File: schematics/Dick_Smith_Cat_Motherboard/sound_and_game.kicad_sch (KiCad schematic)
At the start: 24 parts, among them J8 Joystick, U34 74LS08, U39 74LS374, U42 SN76489AN, U43 74LS138, U45 74LS151, U46 NE558

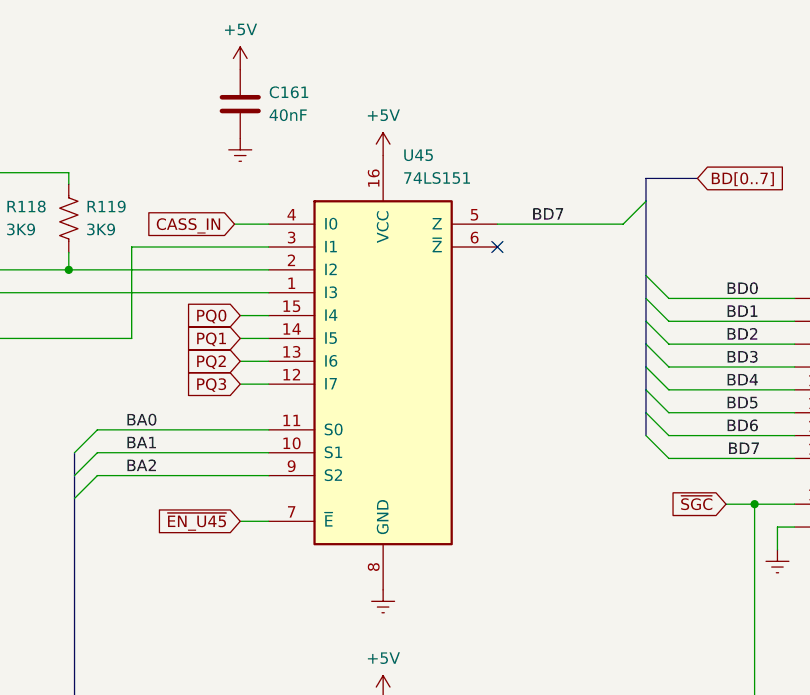
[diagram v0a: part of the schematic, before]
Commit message: Fix chip numbers in the motherboard schematic
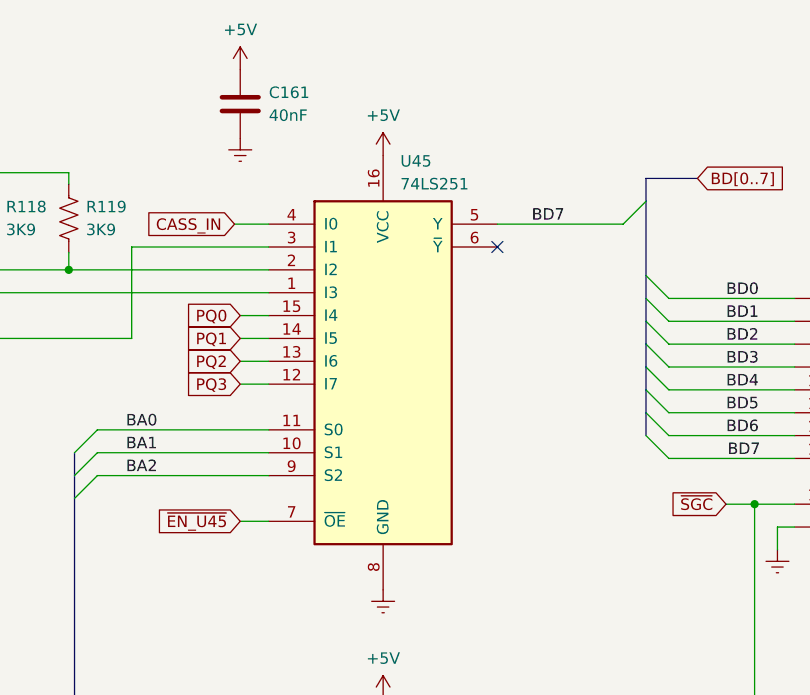
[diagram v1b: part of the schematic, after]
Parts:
- removed U45: 74LS151, Package_DIP:DIP-16_W7.62mm, symbol 74xx:74LS151
- added U45: 74LS251, Package_DIP:DIP-16_W7.62mm, symbol 74xx:74LS251
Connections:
- net +5V: now also U45.16 (VCC)
- net BA0: now also U45.11 (S0)
- net BA1: now also U45.10 (S1)
- net BA2: now also U45.9 (S2)
- net BD7: now also U45.5 (Y)
- net CASS_IN: now also U45.4 (I0)
- net Earth: now also U45.8 (GND)
- net PQ0: now also U45.15 (I4)
- net PQ1: now also U45.14 (I5)
- net PQ2: now also U45.13 (I6)
- net PQ3: now also U45.12 (I7)
- net SW0: now also U45.3 (I1)
- net SW1: now also U45.2 (I2)
- net SW2: now also U45.1 (I3)
- net ~{EN_U45}: now also U45.7 (~{OE})
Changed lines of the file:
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@@
+    )
+  )
+  (symbol (lib_id "74xx:74LS251") (at 115.57 65.405 0) (unit 1)
+    (in_bom yes) (on_board yes) (dnp no)
+    (property "Reference" "U45" (at 117.475 43.18 0)
+      (effects (font (size 1.27 1.27)) (justify left))
+    )
+    (property "Value" "74LS251" (at 117.475 45.72 0)
+      (effects (font (size 1.27 1.27)) (justify left))
+    )
+    (property "Footprint" "Package_DIP:DIP-16_W7.62mm" (at 115.57 65.405 0)
+      (effects (font (size 1.27 1.27)) hide)
+    )
+    (property "Datasheet" "http://www.ti.com/lit/gpn/sn74LS251" (at 115.57 65.405 0)
+      (effects (font (size 1.27 1.27)) hide)
+    )
+    (pin "9")
+    (pin "2")
+    (pin "11")
+    (pin "3")
+    (pin "16")
+    (pin "13")
+    (pin "1")
+    (pin "4")
+    (pin "10")
+    (pin "8")
+    (pin "7")
+    (pin "6")
+    (pin "5")
+    (pin "14")
+    (pin "15")
+    (pin "12")
+    (instances
+      (project "Dick_Smith_Cat_Motherboard"
+        (path "/b825002a-fcdd-4970-89c6-1645cf48180b/e24ea90e-b08a-42db-9a63-e0e6da1adbd2"
+          (reference "U45") (unit 1)
+        )
+      )
     )
   )
@@
         )
       )
-    )
-  )
-  (symbol (lib_id "74xx:74LS151") (at 115.57 65.405 0) (unit 1)
-    (in_bom yes) (on_board yes) (dnp no) (fields_autoplaced)
-    (property "Reference" "U45" (at 117.7641 42.545 0)
-      (effects (font (size 1.27 1.27)) (justify left))
-    )
-    (property "Value" "74LS151" (at 117.7641 45.085 0)
-      (effects (font (size 1.27 1.27)) (justify left))
-    )
-    (property "Footprint" "Package_DIP:DIP-16_W7.62mm" (at 115.57 65.405 0)
-      (effects (font (size 1.27 1.27)) hide)
-    )
-    (property "Datasheet" "http://www.ti.com/lit/gpn/sn74LS151" (at 115.57 65.405 0)
-      (effects (font (size 1.27 1.27)) hide)
-    )
-    (pin "2")
-    (pin "9")
-    (pin "10")
-    (pin "4")
-    (pin "5")
-    (pin "11")
-    (pin "16")
-    (pin "8")
-    (pin "13")
-    (pin "7")
-    (pin "12")
-    (pin "3")
-    (pin "1")
-    (pin "6")
-    (pin "14")
-    (pin "15")
-    (instances
-      (project "Dick_Smith_Cat_Motherboard"
-        (path "/b825002a-fcdd-4970-89c6-1645cf48180b/e24ea90e-b08a-42db-9a63-e0e6da1adbd2"
-          (reference "U45") (unit 1)
-        )
-      )

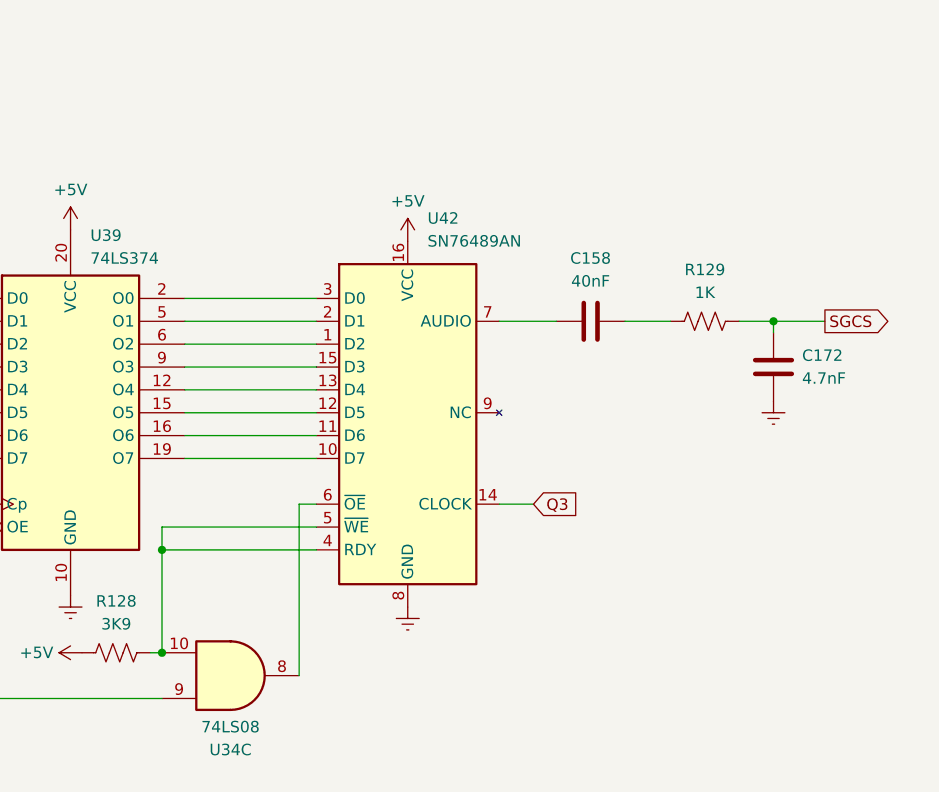
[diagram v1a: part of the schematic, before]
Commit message: Fix pinout of SN76489AN sound chip
The sound chip uses D0 as the MSB.  The bits are swapped in hardware.
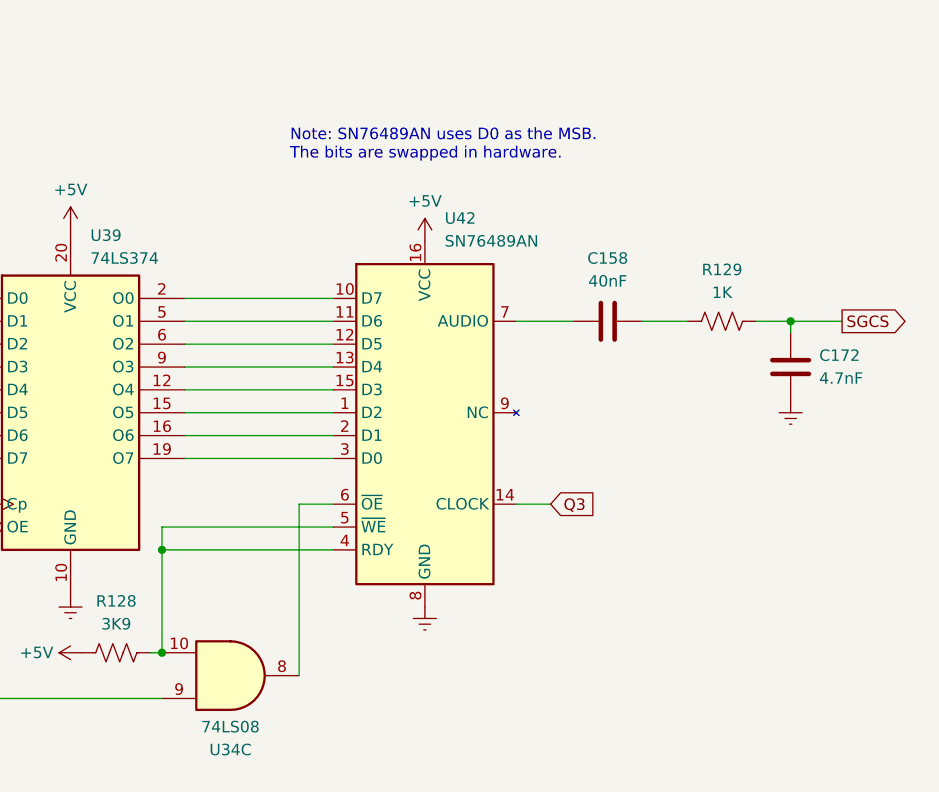
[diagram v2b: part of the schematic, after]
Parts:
- removed U42: SN76489AN, Package_DIP:DIP-16_W7.62mm, symbol VTech:SN76489AN
- added U42: SN76489AN, Package_DIP:DIP-16_W7.62mm, symbol VTech:SN76489AN_Reversed
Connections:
- net +5V: now also U42.16 (VCC)
- net Earth: now also U42.8 (GND)
- net Q3: now also U42.14 (CLOCK)
- net at U39.12 (O4): now also U42.15 (D3)
- net at U39.15 (O5): now also U42.1 (D2)
- net at U39.16 (O6): now also U42.2 (D1)
- net at U39.19 (O7): now also U42.3 (D0)
- net at U39.2 (O0): now also U42.10 (D7)
- net at U39.5 (O1): now also U42.11 (D6)
- net at U39.6 (O2): now also U42.12 (D5)
- net at U39.9 (O3): now also U42.13 (D4)
- net at R128.2, U34.10: now also U42.4 (RDY), U42.5 (~{WE})
- net at U34.8: now also U42.6 (~{OE})
- net at C158.1: now also U42.7 (AUDIO)
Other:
- note added: "Note: SN76489AN uses D0 as the MSB. The bits are swapped in hardware."
- moved on the sheet: C158, C172, R129
